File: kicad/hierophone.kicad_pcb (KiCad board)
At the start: 2 copper layers, 220 x 130 mm, 166 parts, among them J1 AudioJack2_SwitchT, J10 Conn_01x02, J2 AudioJack2_SwitchT, J3 Conn_01x03_Pin, J4 AudioJack2_SwitchT, J5 AudioJack2_SwitchT, J6 AudioJack2_SwitchT, J7 AudioJack2_SwitchT, J8 Conn_01x02, J9 Conn_01x02, Q1 2N3904, Q2 2N3906, Q3 2N3906, SW1 SW_SPDT, SW3 SW_SPDT, U10 TL072, U11 TL072, U12 TL072, U13 TL072, U2 LM13700, U3 LM13700, U4 TL072, U5 TL072, U6 LM386, U7 NE5534, U8 TL072, U9 ICL7660

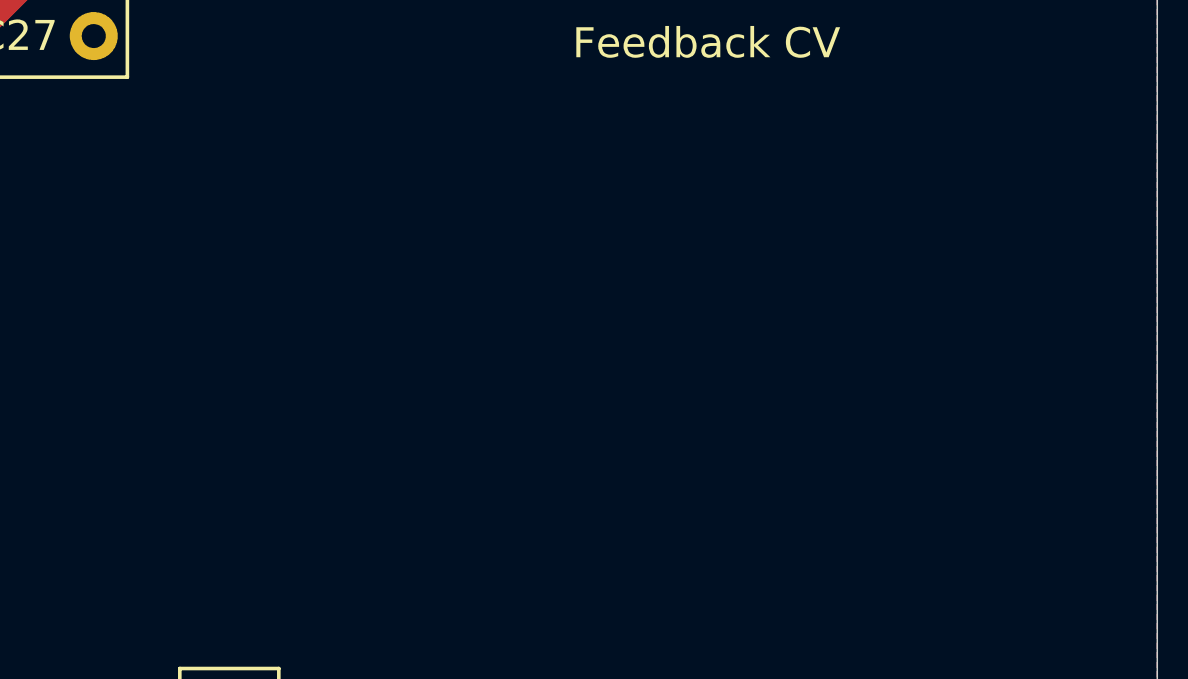
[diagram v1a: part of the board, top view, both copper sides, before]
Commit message: Adding version info text to PCB
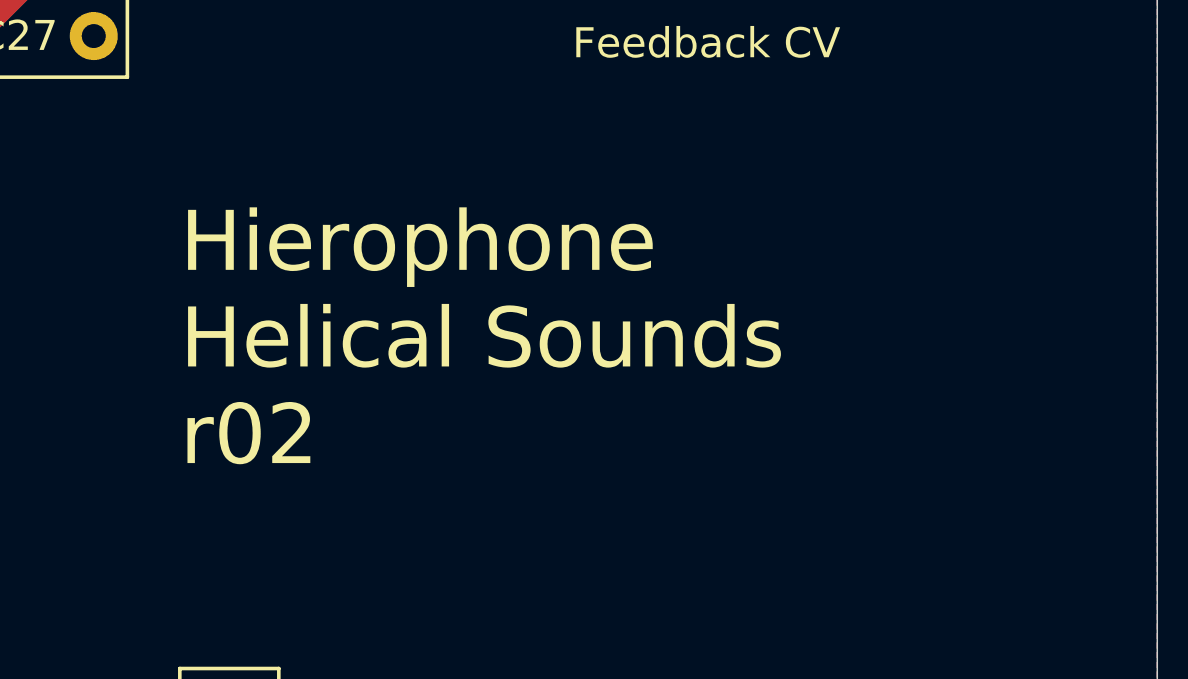
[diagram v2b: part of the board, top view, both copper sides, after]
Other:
- board text added: "${TITLE} ${COMPANY} ${REVISION}"
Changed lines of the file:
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@@
+		)
+	)
+	(gr_text "${TITLE}\n${COMPANY}\n${REVISION}"
+		(at 217.424 88.9 0)
+		(layer "F.SilkS")
+		(effects
+			(font
+				(size 2 2)
+				(thickness 0.15)
+			)
+			(justify left bottom)
 		)
 	)

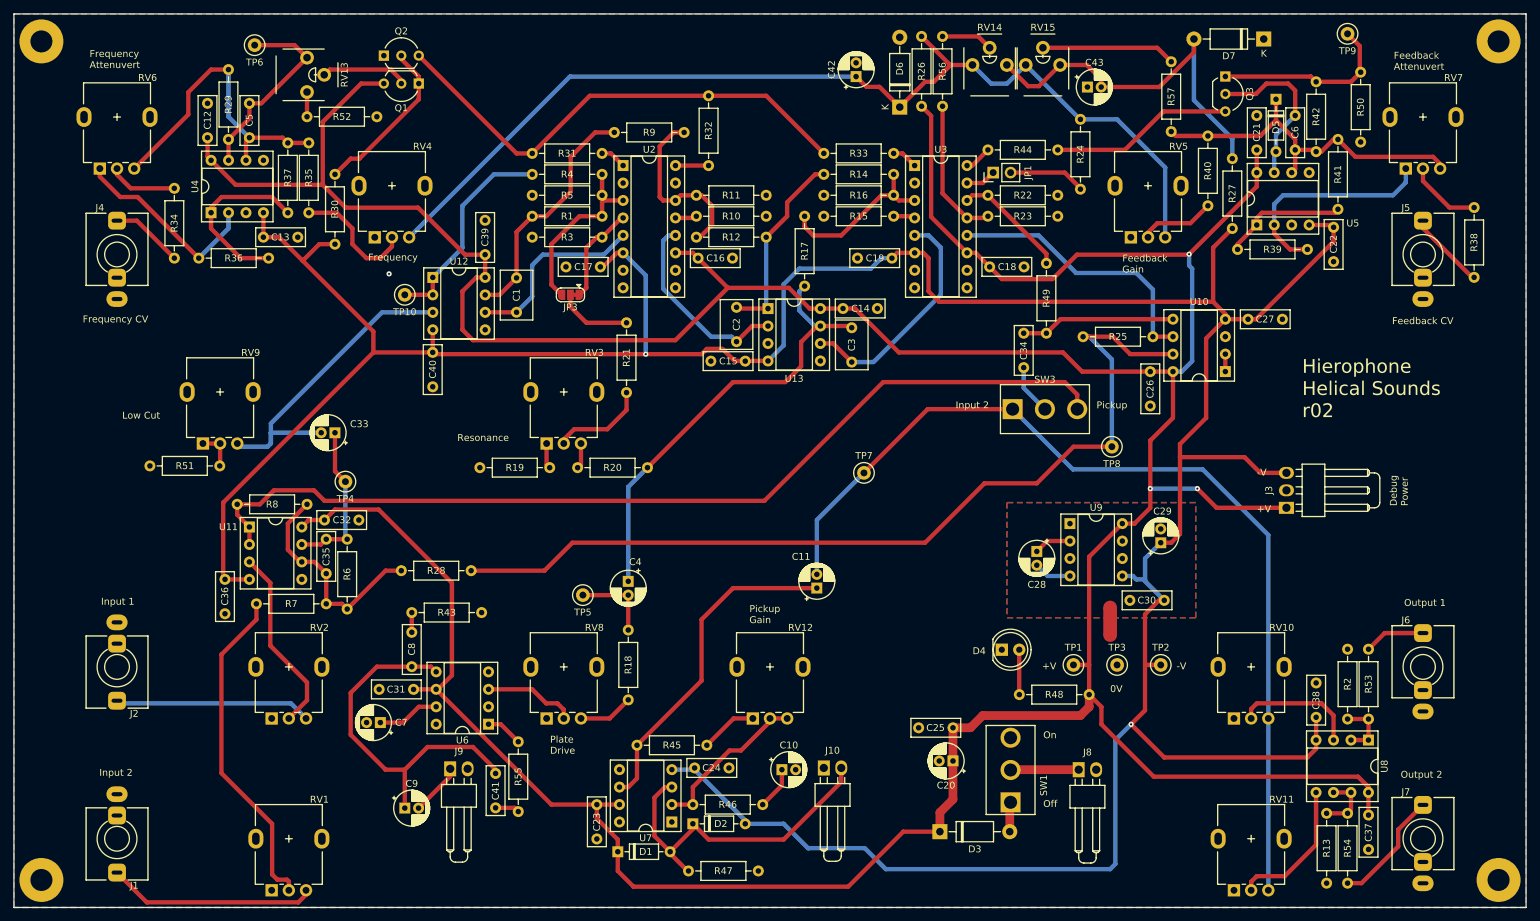
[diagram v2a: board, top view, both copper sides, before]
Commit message: Updating for KiCAD version 9
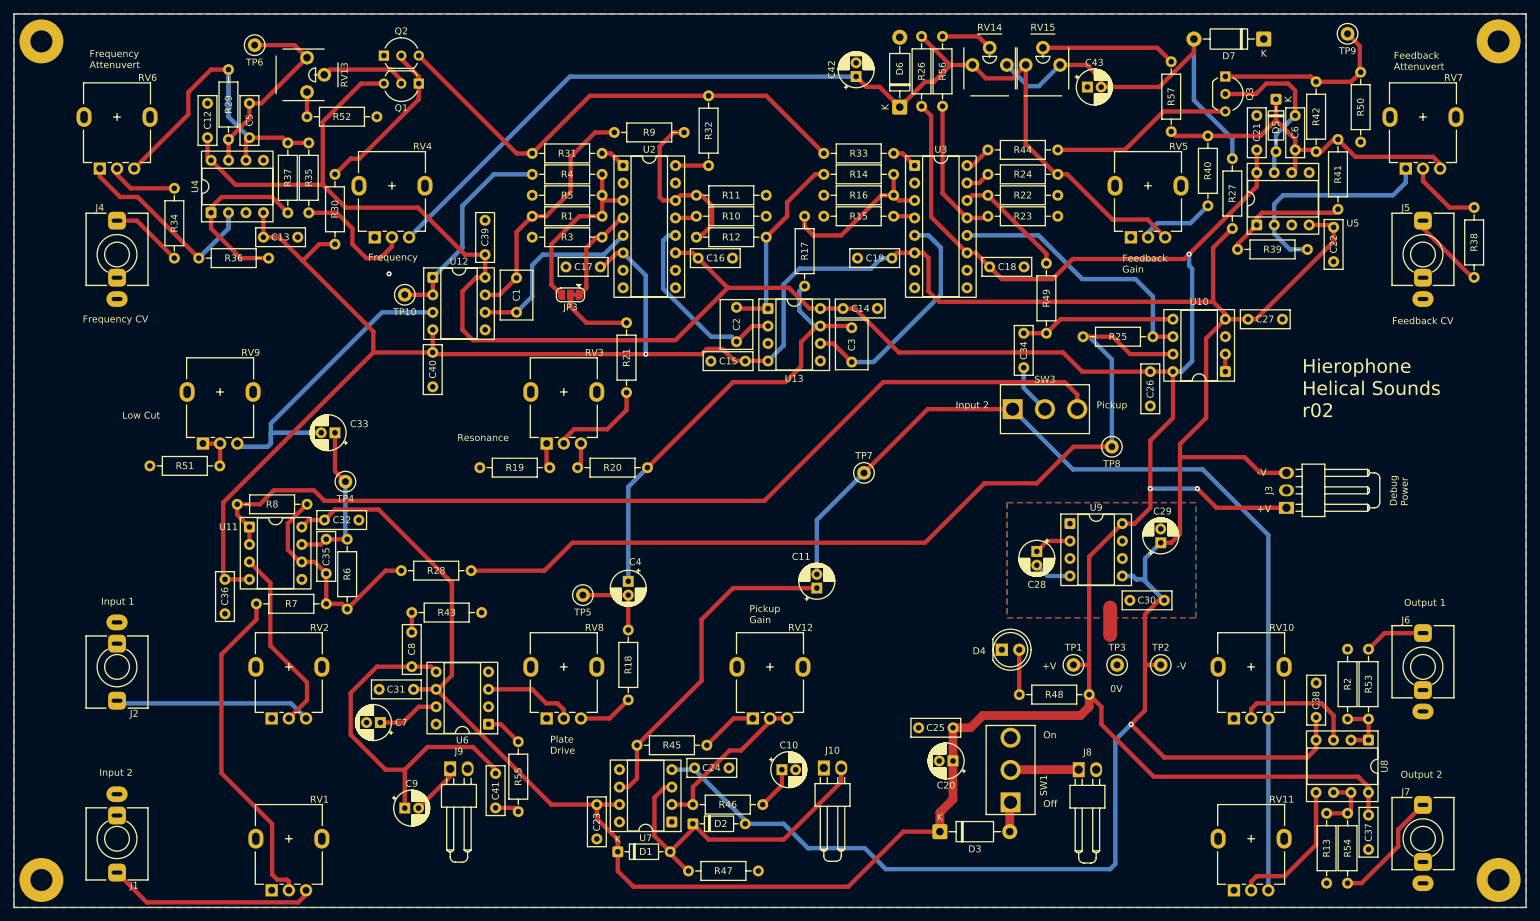
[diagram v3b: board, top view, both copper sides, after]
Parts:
- removed JP1: Jumper_2_Open, Connector_PinHeader_2.54mm:PinHeader_1x02_P2.54mm_Vertical
- moved R24 13.6 mm to (171.7, 53.3), turned to 0 degrees
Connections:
- R24 pad 1: Net-(JP1-B) -> Net-(U3A-DIODE_BIAS)
- U3 pad 15: Net-(JP1-A) -> Net-(U3A-DIODE_BIAS)
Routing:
- net Net-(JP1-B): track 10.4 -> 0.00 mm
- net Net-(JP1-A): track 4.43 -> 0.00 mm
- net Net-(U3A-DIODE_BIAS): track 0.00 -> 3.56 mm
- net Net-(U10B--): track 40.1 -> 39.5 mm

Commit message: Tweaking PCB
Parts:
- removed JP3: Jumper_3_Bridged12, Jumper:SolderJumper-3_P1.3mm_Bridged12_RoundedPad1.0x1.5mm
- added R58: 1k, Rumblesan_Standard_Parts:R_Axial_DIN0207_L6.3mm_D2.5mm_P10.16mm_Horizontal, F.Cu at (222.5, 39.9)
- R18: value 22k -> 47k
- R19: value 47k -> 10k
- R38, R56: value 100k -> 220k
- R39, R41: value 100k -> 10k
- R42: value 33k -> 22k
- R50: value 1k -> 1k2
- R57: value 100k -> 1m
- moved R57 20.1 mm to (180.6, 46.4), turned to 0 degrees
- moved R7 18.6 mm to (78.5, 128.9), turned to 90 degrees
- moved R41 8.88 mm to (225.6, 50.0)
- moved TP9 6.68 mm to (217.6, 34.5)
- moved R50 5.23 mm to (221.2, 36.2), turned to 0 degrees
- moved D7 4.54 mm to (207.8, 35.7)
- moved C43 3.55 mm to (189.4, 39.1), turned to 90 degrees
- moved RV15 2.94 mm to (179.8, 39.1), turned to 180 degrees
- moved C33 2.03 mm to (76.7, 93.0)
- moved C7 2.03 mm to (85.3, 133.1)
- moved RV14 0.40 mm to (172.0, 36.6)
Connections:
- net /NEG_5V_REF renamed NEG_5V_REF
- C42 pad 1: /POS_5V_REF -> POS_5V_REF
- D6 pad 1: /POS_5V_REF -> POS_5V_REF
- R1 pad 2: Net-(JP3-B) -> Net-(U2C-+)
- R21 pad 1: Net-(JP3-C) -> Net-(U2C-+)
- R24 pad 2: /POS_5V_REF -> POS_5V_REF
- R26 pad 2: /POS_5V_REF -> POS_5V_REF
- R4 pad 2: Net-(JP3-B) -> Net-(U2C-+)
- R42 pad 1: Net-(D5-K) -> Net-(R42-Pad1)
- R5 pad 2: Net-(JP3-B) -> Net-(U2C-+)
- RV14 pad 1: /POS_5V_REF -> POS_5V_REF
- RV15 pad 1: /POS_5V_REF -> POS_5V_REF
- RV4 pad 3: /POS_5V_REF -> POS_5V_REF
- RV5 pad 1: GND -> POS_5V_REF
- RV5 pad 3: /POS_5V_REF -> GND
- RV7 pad 1: Net-(U5A--) -> Net-(D5-K)
- RV7 pad 3: Net-(D5-K) -> Net-(U5A--)
- U2 pad 3: Net-(JP3-B) -> Net-(U2C-+)
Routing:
- net /POS_5V_REF: track 148.7 -> 0.00 mm
- net POS_5V_REF: track 0.00 -> 147.0 mm
- net Net-(U2C-+): track 0.00 -> 29.2 mm
- net Net-(JP3-B): track 26.3 -> 0.00 mm
- net Net-(R7-Pad1): track 48.7 -> 32.1 mm
- net Net-(D5-K): track 52.6 -> 67.4 mm
- net Net-(R57-Pad1): track 19.5 -> 6.30 mm
- net Net-(JP3-C): track 11.1 -> 0.00 mm
- net Net-(U2C--): track 14.4 -> 4.22 mm
- net Net-(R39-Pad2): track 18.1 -> 26.6 mm
- net NEG_5V_REF: track 55.5 -> 48.9 mm
- net VEE: track 502.7 -> 508.8 mm
- net Net-(R38-Pad2): track 10.8 -> 15.3 mm
- net Net-(Q3-E): track 27.0 -> 22.5 mm
- net Net-(J2-PadT): track 28.6 -> 32.4 mm
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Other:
- board text removed: "0V"
- board text removed: "Debug Power"
- board text removed: "Feedback Attenuvert"
- board text removed: "Feedback CV"
- board text removed: "Feedback Gain"
- board text removed: "Frequency"
- board text removed: "Frequency Attenuvert"
- board text removed: "Frequency CV"
- board text removed: "Input 1"
- board text removed: "Low Cut"
- board text removed: "Off"
- board text removed: "On"
- board text removed: "Output 1"
- board text removed: "Output 2"
- board text removed: "Pickup Gain"
- board text removed: "Plate Drive"
- board text removed: "Resonance"
